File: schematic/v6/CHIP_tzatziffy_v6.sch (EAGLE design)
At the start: 43 parts, among them J1 2X20-CHIP0.8_DRILL, J3 S2B-PH-SM4-TB, Q1 NPN-DTC114YUA, Q2 PNP-DTA114YUA, U1 LMR62421, U3 DS2431P, X1 FH12-40S-0.5SH

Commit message: added diode on bottom
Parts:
- added D2: B240A, Keyboard v0_5:DIODE_SCHTKY_B240
- added LG, LI, LO, RG, RI, RO: LSP10, solpad:LSP10
- C8, C9: value 100nF -> n.a.
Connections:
- net GND: now also LG.MP, RG.MP
- net PWR_LGT: now also D2.C
- net VREG_OUTPUT: now also D2.A
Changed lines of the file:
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@@
 <part name="U$28" library="Keyboard v0.2" deviceset="GND" device=""/>
 <part name="U$29" library="Keyboard v0.2" deviceset="GND" device=""/>
-<part name="C8" library="rcl" deviceset="C-EU" device="C0805" value="100nF"/>
+<part name="C8" library="rcl" deviceset="C-EU" device="C0805" value="n.a."/>
 <part name="U$30" library="Keyboard v0.2" deviceset="GND" device=""/>
 <part name="U$31" library="Keyboard v0.2" deviceset="GND" device=""/>
-<part name="C9" library="rcl" deviceset="C-EU" device="C0805" value="100nF"/>
+<part name="C9" library="rcl" deviceset="C-EU" device="C0805" value="n.a."/>
 <part name="C7" library="rcl" deviceset="C-EU" device="C0805" value="n.a."/>
 <part name="C10" library="rcl" deviceset="C-EU" device="C0805" value="n.a."/>
@@
 <part name="U$4" library="JKW_CHIP" deviceset="LOGO_NO_TRASH" device="NO_TRASH"/>
 <part name="U$5" library="JKW_CHIP" deviceset="LOGO_10X10_SILK" device=""/>
+<part name="LI" library="solpad" deviceset="LSP10" device=""/>
+<part name="LG" library="solpad" deviceset="LSP10" device=""/>
+<part name="LO" library="solpad" deviceset="LSP10" device=""/>
+<part name="RI" library="solpad" deviceset="LSP10" device=""/>
+<part name="RG" library="solpad" deviceset="LSP10" device=""/>
+<part name="RO" library="solpad" deviceset="LSP10" device=""/>
+<part name="D2" library="Keyboard v0_5" deviceset="DIODE_SCHTKY_B240" device="" value="B240A"/>
 </parts>
 <sheets>
@@
 <instance part="U$4" gate="G$1" x="279.4" y="50.8"/>
 <instance part="U$5" gate="G$1" x="279.4" y="43.18"/>
+<instance part="LI" gate="1" x="353.06" y="271.78"/>
+<instance part="LG" gate="1" x="363.22" y="271.78"/>
+<instance part="LO" gate="1" x="358.14" y="271.78"/>
+<instance part="RI" gate="1" x="378.46" y="266.7"/>
+<instance part="RG" gate="1" x="370.84" y="271.78"/>
+<instance part="RO" gate="1" x="381" y="271.78"/>
+<instance part="D2" gate="G$1" x="535.94" y="271.78"/>
 </instances>
 <busses>
@@
 <pinref part="GND7" gate="1" pin="GND"/>
 <wire x1="325.12" y1="259.08" x2="347.98" y2="259.08" width="0.1524" layer="91"/>
-<wire x1="347.98" y1="259.08" x2="373.38" y2="259.08" width="0.1524" layer="91"/>
+<wire x1="347.98" y1="259.08" x2="363.22" y2="259.08" width="0.1524" layer="91"/>
+<wire x1="363.22" y1="259.08" x2="370.84" y2="259.08" width="0.1524" layer="91"/>
+<wire x1="370.84" y1="259.08" x2="373.38" y2="259.08" width="0.1524" layer="91"/>
 <wire x1="373.38" y1="259.08" x2="373.38" y2="256.54" width="0.1524" layer="91"/>
 <pinref part="C12" gate="G$1" pin="1"/>
 <wire x1="347.98" y1="256.54" x2="347.98" y2="259.08" width="0.1524" layer="91"/>
 <junction x="347.98" y="259.08"/>
+<pinref part="LG" gate="1" pin="MP"/>
+<wire x1="363.22" y1="269.24" x2="363.22" y2="259.08" width="0.1524" layer="91"/>
+<junction x="363.22" y="259.08"/>
+<pinref part="RG" gate="1" pin="MP"/>
+<wire x1="370.84" y1="269.24" x2="370.84" y2="259.08" width="0.1524" layer="91"/>
+<junction x="370.84" y="259.08"/>
 </segment>
 <segment>
@@
 <junction x="568.96" y="261.62"/>
 <pinref part="D1" gate="G$1" pin="C"/>
-<wire x1="538.48" y1="261.62" x2="543.56" y2="261.62" width="0.1524" layer="91"/>
+<wire x1="538.48" y1="261.62" x2="541.02" y2="261.62" width="0.1524" layer="91"/>
+<wire x1="541.02" y1="261.62" x2="543.56" y2="261.62" width="0.1524" layer="91"/>
 <wire x1="581.66" y1="228.854" x2="580.39" y2="228.346" width="0.1524" layer="91"/>
 <pinref part="Q2" gate="G$1" pin="GND"/>
+<pinref part="D2" gate="G$1" pin="C"/>
+<wire x1="538.48" y1="271.78" x2="541.02" y2="271.78" width="0.1524" layer="91"/>
+<wire x1="541.02" y1="271.78" x2="541.02" y2="261.62" width="0.1524" layer="91"/>
+<junction x="541.02" y="261.62"/>
 </segment>
 </net>
@@
 <pinref part="L1" gate="G$1" pin="1"/>
 <wire x1="525.78" y1="269.24" x2="515.62" y2="269.24" width="0.1524" layer="91"/>
-<wire x1="525.78" y1="261.62" x2="533.4" y2="261.62" width="0.1524" layer="91"/>
+<wire x1="525.78" y1="261.62" x2="530.86" y2="261.62" width="0.1524" layer="91"/>
 <pinref part="D1" gate="G$1" pin="A"/>
 <pinref part="L2" gate="G$1" pin="1"/>
+<wire x1="530.86" y1="261.62" x2="533.4" y2="261.62" width="0.1524" layer="91"/>
 <wire x1="515.62" y1="276.86" x2="525.78" y2="276.86" width="0.1524" layer="91"/>
 <wire x1="525.78" y1="276.86" x2="525.78" y2="269.24" width="0.1524" layer="91"/>
 <junction x="525.78" y="269.24"/>
-</segment>
-</net>
+<wire x1="530.86" y1="261.62" x2="530.86" y2="271.78" width="0.1524" layer="91"/>
+<pinref part="D2" gate="G$1" pin="A"/>
+<wire x1="530.86" y1="271.78" x2="533.4" y2="271.78" width="0.1524" layer="91"/>
+<junction x="530.86" y="261.62"/>
+</segment>
+</net>

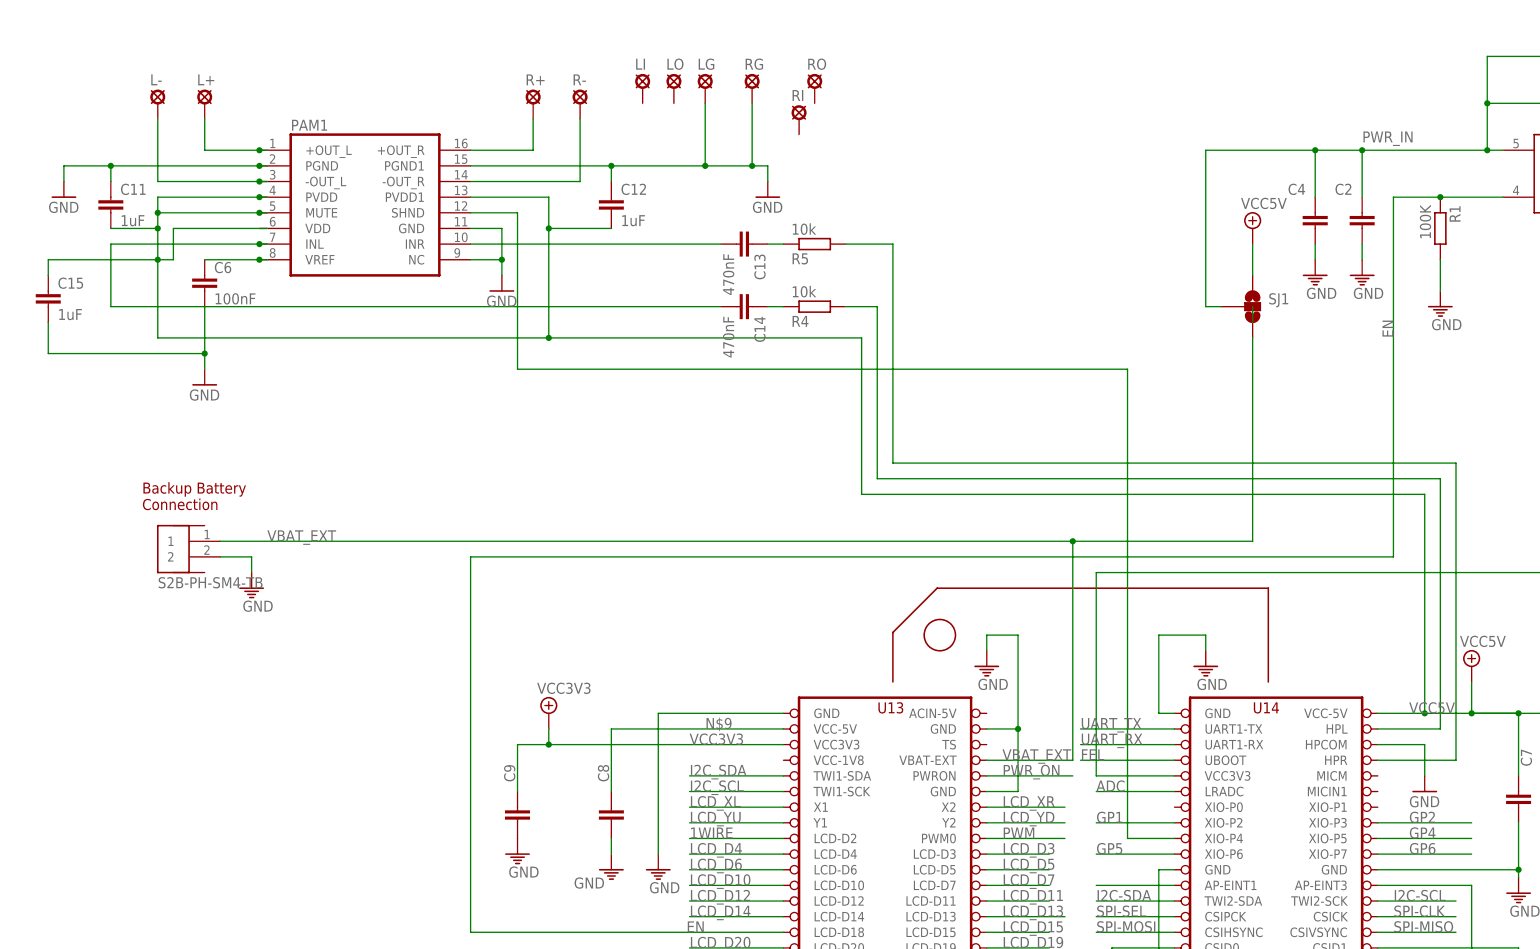
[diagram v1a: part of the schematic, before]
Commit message: Added connection for poti
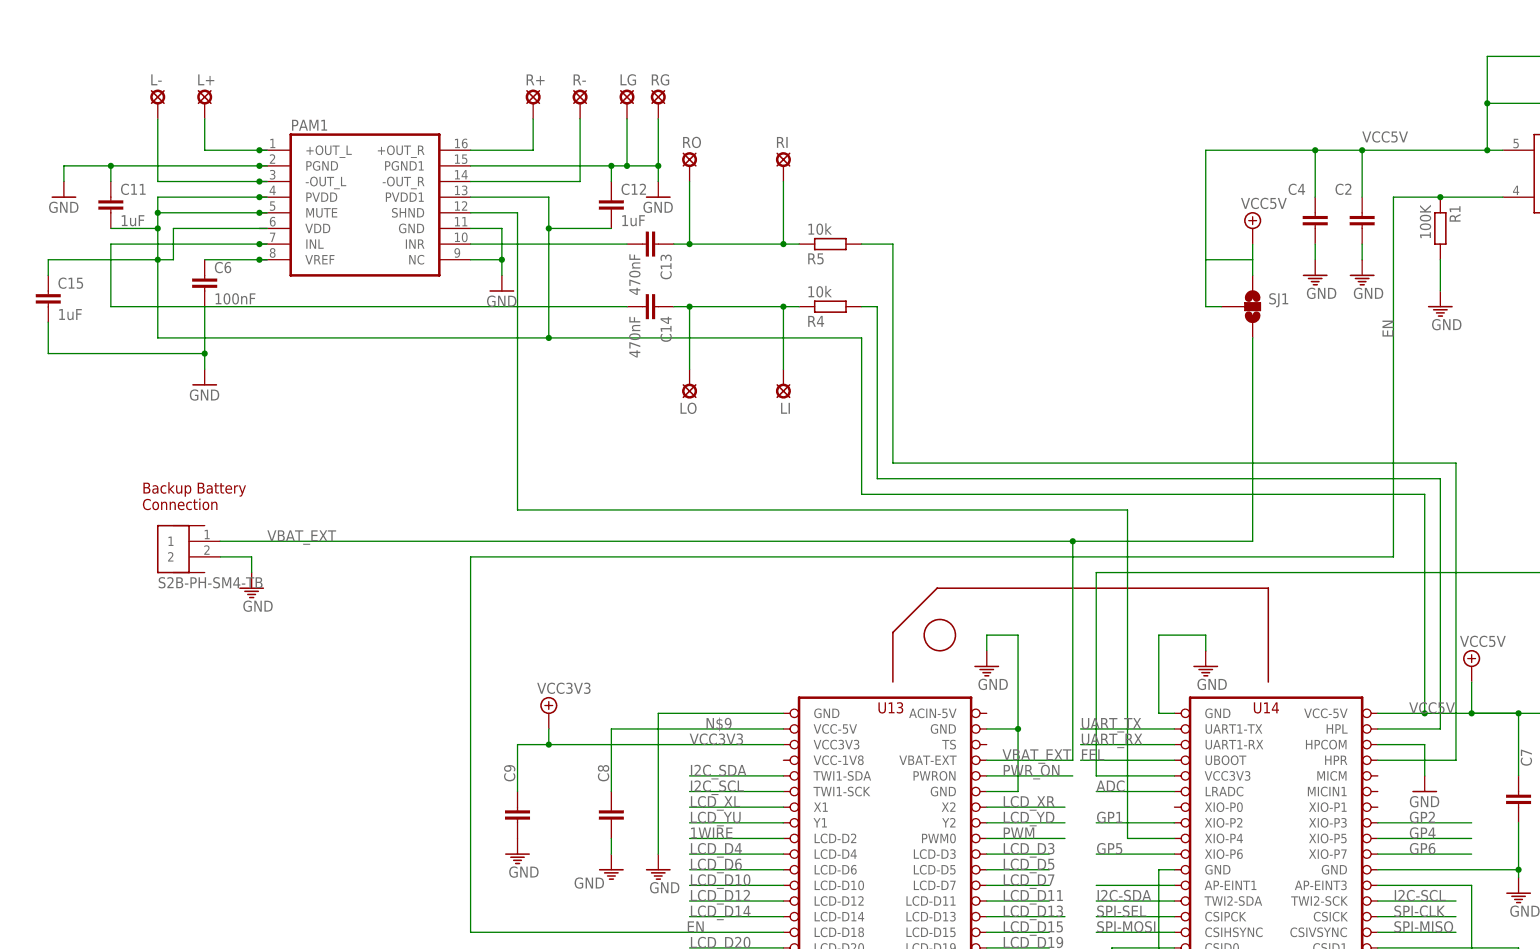
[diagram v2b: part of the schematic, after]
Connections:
- removed net N$42: C14.1, R4.1
- removed net PWR_IN: C2.1, C4.1, L1.2, L2.2, SJ1.2, U1.VIN
- new net N$43: C13.1, R5.1, RI.MP, RO.MP
- net N$41: now also C14.1, LI.MP, LO.MP, R4.1; no longer C13.1, R5.1
- net VCC5V: now also C2.1, C4.1, L1.2, L2.2, SJ1.2, U1.VIN
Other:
- note added: "<- cut here"
- note added: "cut here"
- moved on the sheet: C13, C14, LG, LI, LO, R4, R5, RG, RI, RO

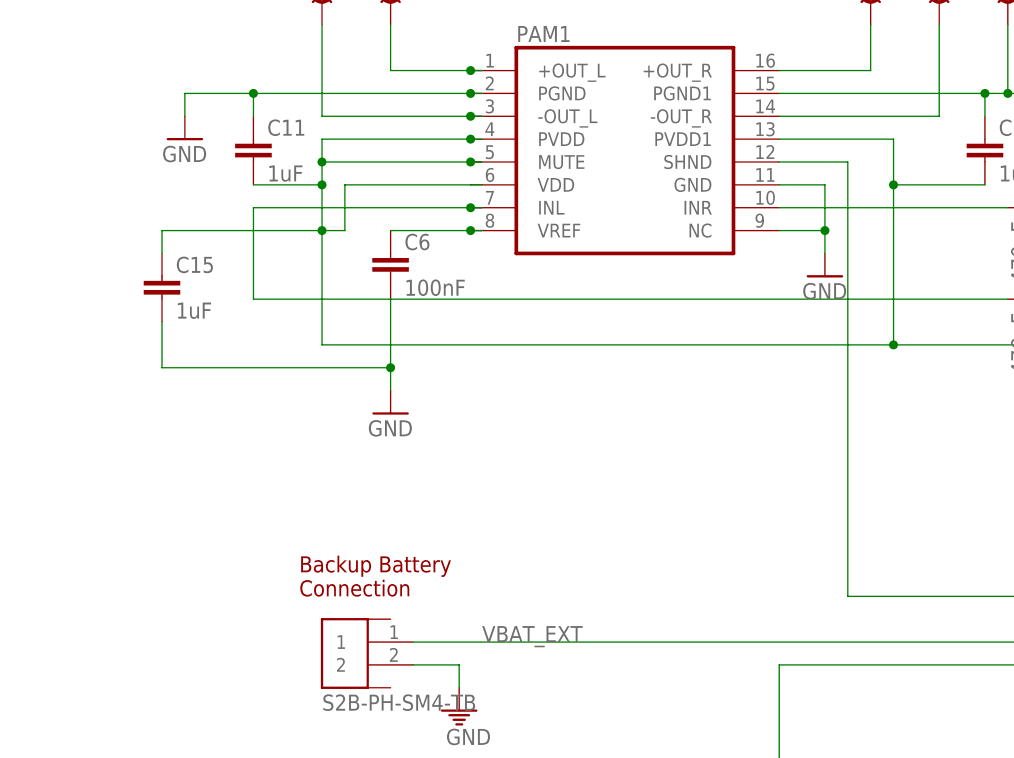
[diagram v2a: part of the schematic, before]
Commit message: added pulldown for shutdown
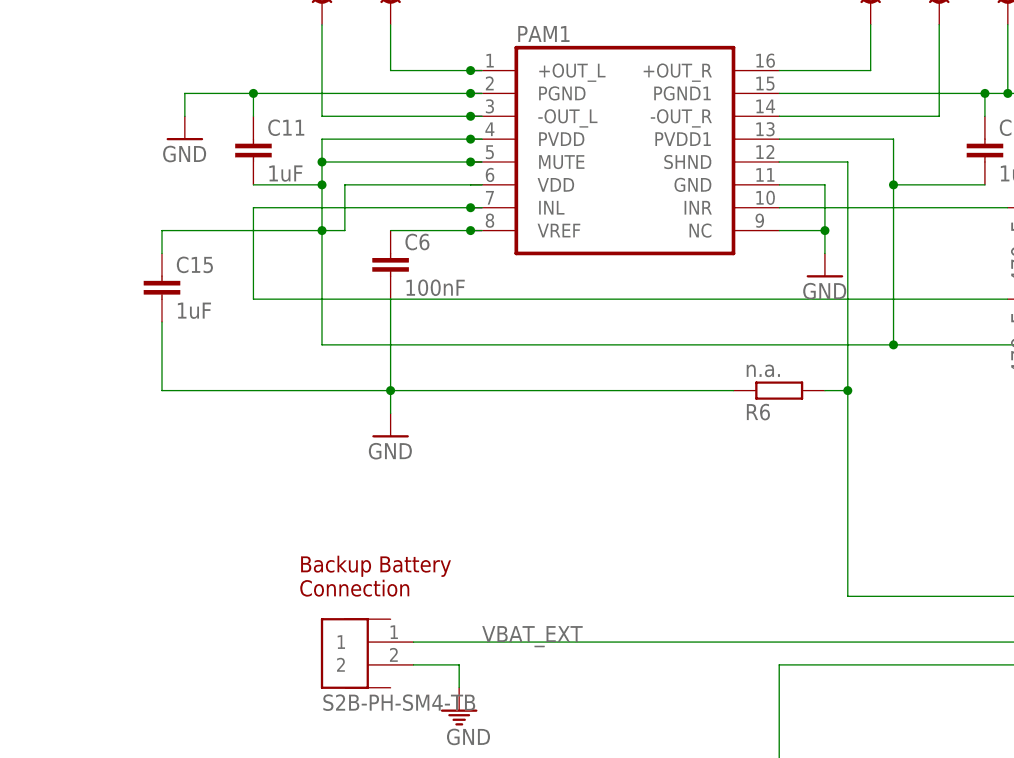
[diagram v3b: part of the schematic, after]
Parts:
- added R6: n.a., rcl:R-EU_R0805
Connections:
- net GND: now also R6.1
- net GP3: now also R6.2
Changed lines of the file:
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@@
 <part name="RO" library="solpad" deviceset="LSP10" device=""/>
 <part name="D2" library="Keyboard v0_5" deviceset="DIODE_SCHTKY_B240" device="" value="B240A"/>
+<part name="R6" library="rcl" deviceset="R-EU_" device="R0805" value="n.a."/>
 </parts>
 <sheets>
@@
 <instance part="GND8" gate="1" x="330.2" y="238.76"/>
 <instance part="C6" gate="G$1" x="281.94" y="241.3"/>
-<instance part="GND9" gate="1" x="281.94" y="223.52"/>
+<instance part="GND9" gate="1" x="281.94" y="220.98"/>
 <instance part="C11" gate="G$1" x="266.7" y="254"/>
 <instance part="C12" gate="G$1" x="347.98" y="254"/>
@@
 <instance part="RO" gate="1" x="360.68" y="259.08"/>
 <instance part="D2" gate="G$1" x="535.94" y="271.78"/>
+<instance part="R6" gate="G$1" x="325.12" y="226.06" rot="MR180"/>
 </instances>
 <busses>
@@
 <wire x1="431.8" y1="149.86" x2="431.8" y2="203.2" width="0.1524" layer="91"/>
 <wire x1="431.8" y1="203.2" x2="332.74" y2="203.2" width="0.1524" layer="91"/>
-<wire x1="332.74" y1="203.2" x2="332.74" y2="251.46" width="0.1524" layer="91"/>
+<wire x1="332.74" y1="203.2" x2="332.74" y2="226.06" width="0.1524" layer="91"/>
 <pinref part="PAM1" gate="G$1" pin="SHND"/>
+<wire x1="332.74" y1="226.06" x2="332.74" y2="251.46" width="0.1524" layer="91"/>
 <wire x1="332.74" y1="251.46" x2="325.12" y2="251.46" width="0.1524" layer="91"/>
+<pinref part="R6" gate="G$1" pin="2"/>
+<wire x1="330.2" y1="226.06" x2="332.74" y2="226.06" width="0.1524" layer="91"/>
+<junction x="332.74" y="226.06"/>
 </segment>
 </net>
@@
 <pinref part="C6" gate="G$1" pin="2"/>
 <pinref part="GND9" gate="1" pin="GND"/>
-<wire x1="281.94" y1="236.22" x2="281.94" y2="228.6" width="0.1524" layer="91"/>
+<wire x1="281.94" y1="236.22" x2="281.94" y2="226.06" width="0.1524" layer="91"/>
 <pinref part="C15" gate="G$1" pin="2"/>
-<wire x1="281.94" y1="228.6" x2="281.94" y2="226.06" width="0.1524" layer="91"/>
-<wire x1="256.54" y1="233.68" x2="256.54" y2="228.6" width="0.1524" layer="91"/>
-<wire x1="256.54" y1="228.6" x2="281.94" y2="228.6" width="0.1524" layer="91"/>
-<junction x="281.94" y="228.6"/>
-</segment>
-<segment>
+<wire x1="281.94" y1="226.06" x2="281.94" y2="223.52" width="0.1524" layer="91"/>
+<wire x1="256.54" y1="233.68" x2="256.54" y2="226.06" width="0.1524" layer="91"/>
+<wire x1="256.54" y1="226.06" x2="281.94" y2="226.06" width="0.1524" layer="91"/>
+<junction x="281.94" y="226.06"/>
+<wire x1="281.94" y1="226.06" x2="320.04" y2="226.06" width="0.1524" layer="91"/>
+<pinref part="R6" gate="G$1" pin="1"/>
+</segment>
+<segment>

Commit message: added note for pulldown
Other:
- note added: "3mA max -> min 1.1k"
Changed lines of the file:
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@@
 <layer number="59" name="tCarbon" color="7" fill="1" visible="no" active="no"/>
 <layer number="60" name="bCarbon" color="7" fill="1" visible="no" active="no"/>
-<layer number="90" name="Modules" color="5" fill="1" visible="no" active="yes"/>
+<layer number="90" name="Modules" color="5" fill="1" visible="yes" active="yes"/>
 <layer number="91" name="Nets" color="2" fill="1" visible="yes" active="yes"/>
 <layer number="92" name="Busses" color="1" fill="1" visible="yes" active="yes"/>
@@
 <text x="363.22" y="236.22" size="1.778" layer="99">cut here</text>
 <text x="449.58" y="243.84" size="1.778" layer="99" rot="R90">&lt;- cut here</text>
+<text x="304.8" y="220.98" size="1.778" layer="90">3mA max -&gt; min 1.1k </text>
 </plain>
 <instances>

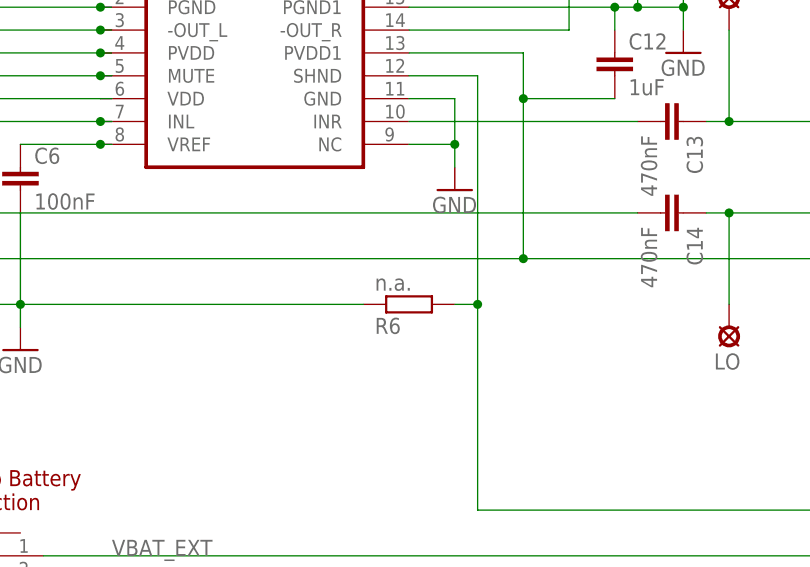
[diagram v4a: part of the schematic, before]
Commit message: changed pulldown to assembled
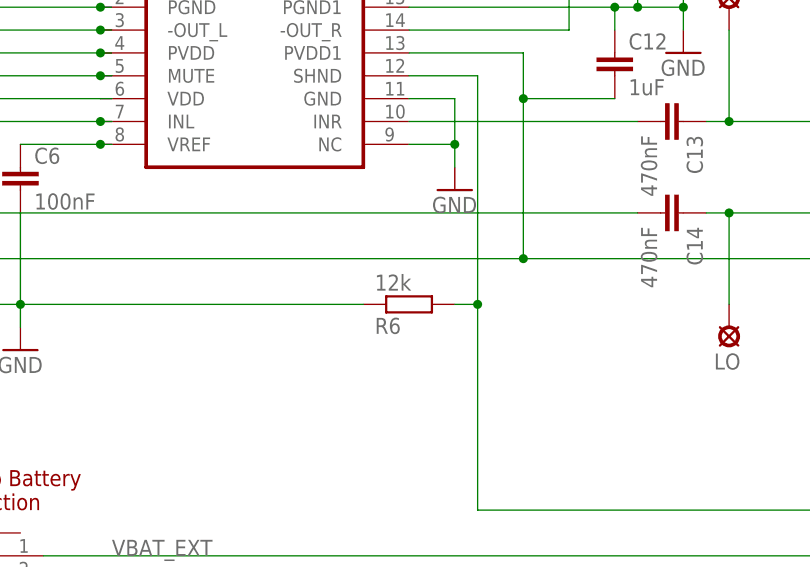
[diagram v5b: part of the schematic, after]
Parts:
- R6: value n.a. -> 12k
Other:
- note removed: "3mA max -> min 1.1k"
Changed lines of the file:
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@@
 <part name="RO" library="solpad" deviceset="LSP10" device=""/>
 <part name="D2" library="Keyboard v0_5" deviceset="DIODE_SCHTKY_B240" device="" value="B240A"/>
-<part name="R6" library="rcl" deviceset="R-EU_" device="R0805" value="n.a."/>
+<part name="R6" library="rcl" deviceset="R-EU_" device="R0805" value="12k"/>
 </parts>
 <sheets>
@@
 <text x="363.22" y="236.22" size="1.778" layer="99">cut here</text>
 <text x="449.58" y="243.84" size="1.778" layer="99" rot="R90">&lt;- cut here</text>
-<text x="304.8" y="220.98" size="1.778" layer="90">3mA max -&gt; min 1.1k </text>
 </plain>
 <instances>
